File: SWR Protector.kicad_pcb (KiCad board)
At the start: 2 copper layers, 100 x 100 mm, 34 parts, among them J1 Barrel_Jack, J2 Barrel_Jack, J3 transceiver, J4 antenna, J5 header, K2 ATX209, Q1 2N3904, T1 1:12, T2 1:12, U1 LM78L05_TO92, U2 LM358

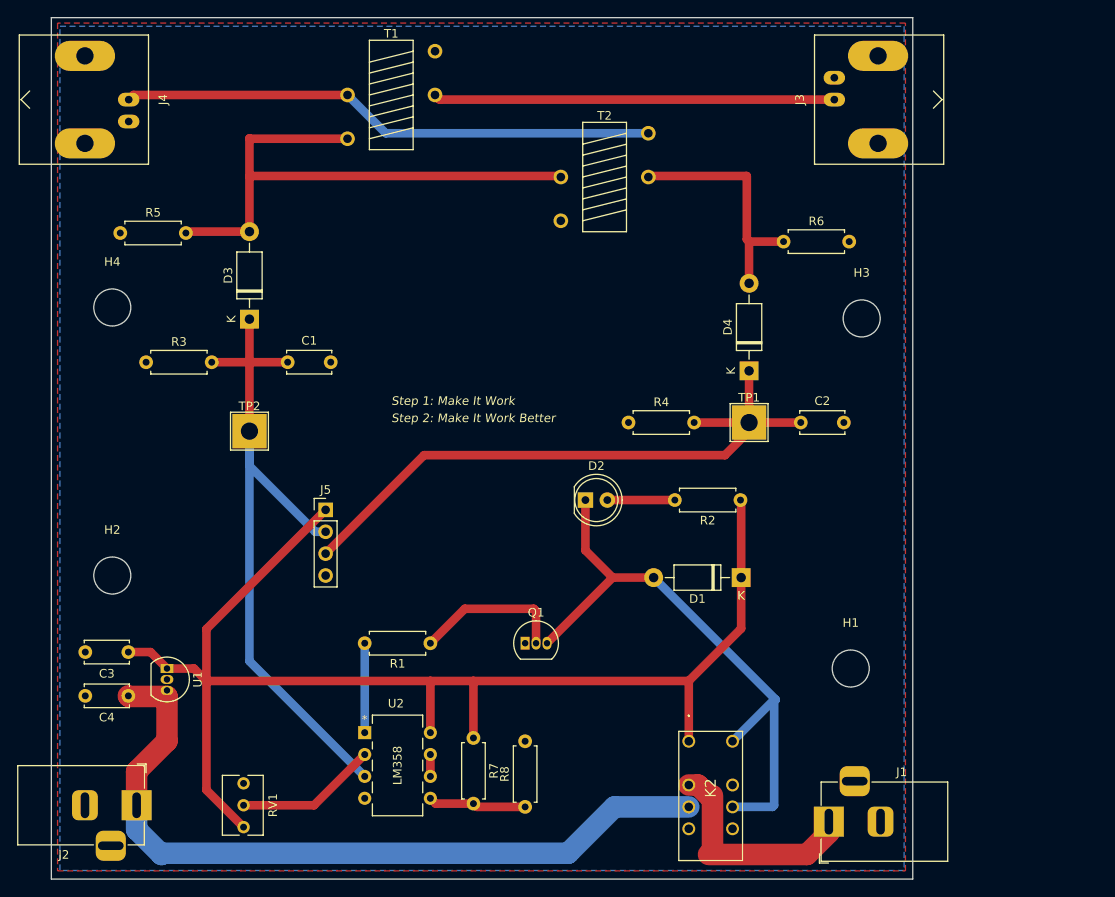
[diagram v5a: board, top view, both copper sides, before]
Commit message: learned how to do via stitching, but the array lands over everything so I spent a lot of time finding and fixing errors (ground via punching right thru power trace, for instance).  Next time the via stitching MUST BE THE LAST STEP IN BOARD DESIGN as any changes at this point will be painful.
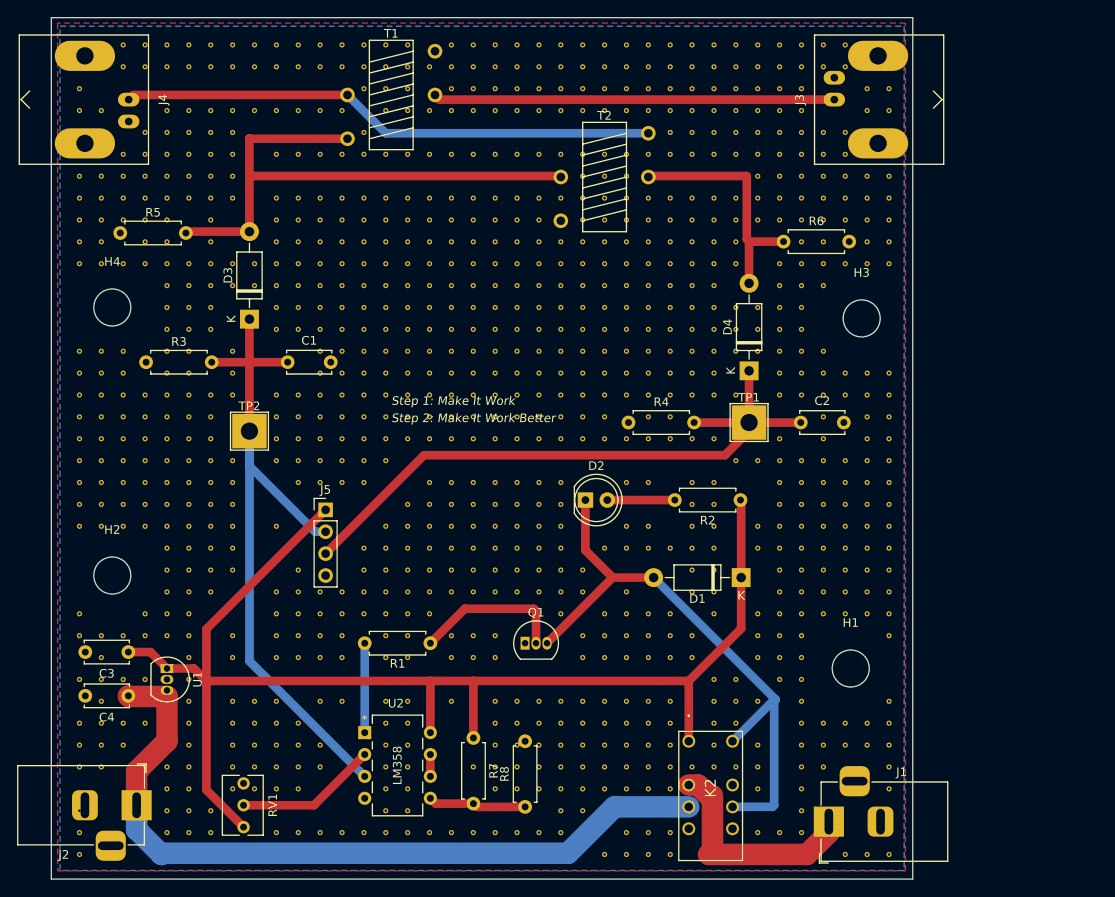
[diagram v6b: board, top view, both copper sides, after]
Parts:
- added REF**10: VIA-0.6mm, MyLibrary:VIA-0.6mm, F.Cu at (113.7, 50.2)
- added REF**100: VIA-0.6mm, MyLibrary:VIA-0.6mm, F.Cu at (149.2, 55.2)
- added REF**1000: VIA-0.6mm, MyLibrary:VIA-0.6mm, F.Cu at (118.7, 116.2)
- added REF**1001: VIA-0.6mm, MyLibrary:VIA-0.6mm, F.Cu at (121.3, 116.2)
- added REF**1002: VIA-0.6mm, MyLibrary:VIA-0.6mm, F.Cu at (123.8, 116.2)
- added REF**1003: VIA-0.6mm, MyLibrary:VIA-0.6mm, F.Cu at (126.4, 116.2)
- added REF**1004: VIA-0.6mm, MyLibrary:VIA-0.6mm, F.Cu at (128.9, 116.2)
- added REF**101: VIA-0.6mm, MyLibrary:VIA-0.6mm, F.Cu at (151.8, 55.2)
- added REF**1010: VIA-0.6mm, MyLibrary:VIA-0.6mm, F.Cu at (144.1, 116.2)
- added REF**1012: VIA-0.6mm, MyLibrary:VIA-0.6mm, F.Cu at (149.2, 116.2)
- added REF**1013: VIA-0.6mm, MyLibrary:VIA-0.6mm, F.Cu at (151.8, 116.2)
- added REF**1014: VIA-0.6mm, MyLibrary:VIA-0.6mm, F.Cu at (154.3, 116.2)
- added REF**1015: VIA-0.6mm, MyLibrary:VIA-0.6mm, F.Cu at (156.8, 116.2)
- added REF**1017: VIA-0.6mm, MyLibrary:VIA-0.6mm, F.Cu at (161.9, 116.2)
- added REF**1019: VIA-0.6mm, MyLibrary:VIA-0.6mm, F.Cu at (167.0, 116.2)
- added REF**102: VIA-0.6mm, MyLibrary:VIA-0.6mm, F.Cu at (154.3, 55.2)
- added REF**1020: VIA-0.6mm, MyLibrary:VIA-0.6mm, F.Cu at (169.5, 116.2)
- added REF**1021: VIA-0.6mm, MyLibrary:VIA-0.6mm, F.Cu at (172.1, 116.2)
- added REF**1022: VIA-0.6mm, MyLibrary:VIA-0.6mm, F.Cu at (174.6, 116.2)
- added REF**1023: VIA-0.6mm, MyLibrary:VIA-0.6mm, F.Cu at (177.2, 116.2)
- added REF**1024: VIA-0.6mm, MyLibrary:VIA-0.6mm, F.Cu at (179.7, 116.2)
- added REF**1025: VIA-0.6mm, MyLibrary:VIA-0.6mm, F.Cu at (182.2, 116.2)
- added REF**1026: VIA-0.6mm, MyLibrary:VIA-0.6mm, F.Cu at (88.3, 118.7)
- added REF**1027: VIA-0.6mm, MyLibrary:VIA-0.6mm, F.Cu at (90.8, 118.7)
- added REF**1028: VIA-0.6mm, MyLibrary:VIA-0.6mm, F.Cu at (93.3, 118.7)
- added REF**1029: VIA-0.6mm, MyLibrary:VIA-0.6mm, F.Cu at (95.9, 118.7)
- added REF**103: VIA-0.6mm, MyLibrary:VIA-0.6mm, F.Cu at (156.8, 55.2)
- added REF**1030: VIA-0.6mm, MyLibrary:VIA-0.6mm, F.Cu at (98.4, 118.7)
- added REF**1031: VIA-0.6mm, MyLibrary:VIA-0.6mm, F.Cu at (101.0, 118.7)
- added REF**1033: VIA-0.6mm, MyLibrary:VIA-0.6mm, F.Cu at (106.0, 118.7)
- added REF**1035: VIA-0.6mm, MyLibrary:VIA-0.6mm, F.Cu at (111.1, 118.7)
- added REF**1036: VIA-0.6mm, MyLibrary:VIA-0.6mm, F.Cu at (113.7, 118.7)
- added REF**1037: VIA-0.6mm, MyLibrary:VIA-0.6mm, F.Cu at (116.2, 118.7)
- added REF**1038: VIA-0.6mm, MyLibrary:VIA-0.6mm, F.Cu at (118.7, 118.7)
- added REF**104: VIA-0.6mm, MyLibrary:VIA-0.6mm, F.Cu at (159.4, 55.2)
- added REF**1040: VIA-0.6mm, MyLibrary:VIA-0.6mm, F.Cu at (123.8, 118.7)
- added REF**1041: VIA-0.6mm, MyLibrary:VIA-0.6mm, F.Cu at (126.4, 118.7)
- added REF**1043: VIA-0.6mm, MyLibrary:VIA-0.6mm, F.Cu at (131.4, 118.7)
- added REF**1044: VIA-0.6mm, MyLibrary:VIA-0.6mm, F.Cu at (134.0, 118.7)
- added REF**1045: VIA-0.6mm, MyLibrary:VIA-0.6mm, F.Cu at (136.5, 118.7)
- added REF**1049: VIA-0.6mm, MyLibrary:VIA-0.6mm, F.Cu at (146.7, 118.7)
- added REF**105: VIA-0.6mm, MyLibrary:VIA-0.6mm, F.Cu at (161.9, 55.2)
- added REF**1050: VIA-0.6mm, MyLibrary:VIA-0.6mm, F.Cu at (149.2, 118.7)
- added REF**1051: VIA-0.6mm, MyLibrary:VIA-0.6mm, F.Cu at (151.8, 118.7)
- added REF**1052: VIA-0.6mm, MyLibrary:VIA-0.6mm, F.Cu at (154.3, 118.7)
- added REF**1053: VIA-0.6mm, MyLibrary:VIA-0.6mm, F.Cu at (156.8, 118.7)
- added REF**1054: VIA-0.6mm, MyLibrary:VIA-0.6mm, F.Cu at (159.4, 118.7)
- added REF**1057: VIA-0.6mm, MyLibrary:VIA-0.6mm, F.Cu at (167.0, 118.7)
- added REF**1058: VIA-0.6mm, MyLibrary:VIA-0.6mm, F.Cu at (169.5, 118.7)
- added REF**1059: VIA-0.6mm, MyLibrary:VIA-0.6mm, F.Cu at (172.1, 118.7)
- added REF**106: VIA-0.6mm, MyLibrary:VIA-0.6mm, F.Cu at (164.5, 55.2)
- added REF**1063: VIA-0.6mm, MyLibrary:VIA-0.6mm, F.Cu at (182.2, 118.7)
- added REF**1065: VIA-0.6mm, MyLibrary:VIA-0.6mm, F.Cu at (90.8, 121.3)
- added REF**1069: VIA-0.6mm, MyLibrary:VIA-0.6mm, F.Cu at (101.0, 121.3)
- added REF**107: VIA-0.6mm, MyLibrary:VIA-0.6mm, F.Cu at (167.0, 55.2)
- added REF**1071: VIA-0.6mm, MyLibrary:VIA-0.6mm, F.Cu at (106.0, 121.3)
- added REF**1073: VIA-0.6mm, MyLibrary:VIA-0.6mm, F.Cu at (111.1, 121.3)
- added REF**1074: VIA-0.6mm, MyLibrary:VIA-0.6mm, F.Cu at (113.7, 121.3)
- added REF**1075: VIA-0.6mm, MyLibrary:VIA-0.6mm, F.Cu at (116.2, 121.3)
- added REF**1076: VIA-0.6mm, MyLibrary:VIA-0.6mm, F.Cu at (118.7, 121.3)
- added REF**1078: VIA-0.6mm, MyLibrary:VIA-0.6mm, F.Cu at (123.8, 121.3)
- added REF**1079: VIA-0.6mm, MyLibrary:VIA-0.6mm, F.Cu at (126.4, 121.3)
- added REF**108: VIA-0.6mm, MyLibrary:VIA-0.6mm, F.Cu at (169.5, 55.2)
- added REF**1081: VIA-0.6mm, MyLibrary:VIA-0.6mm, F.Cu at (131.4, 121.3)
- added REF**1082: VIA-0.6mm, MyLibrary:VIA-0.6mm, F.Cu at (134.0, 121.3)
- added REF**1083: VIA-0.6mm, MyLibrary:VIA-0.6mm, F.Cu at (136.5, 121.3)
- added REF**1087: VIA-0.6mm, MyLibrary:VIA-0.6mm, F.Cu at (146.7, 121.3)
- added REF**1088: VIA-0.6mm, MyLibrary:VIA-0.6mm, F.Cu at (149.2, 121.3)
- added REF**1089: VIA-0.6mm, MyLibrary:VIA-0.6mm, F.Cu at (151.8, 121.3)
- added REF**109: VIA-0.6mm, MyLibrary:VIA-0.6mm, F.Cu at (172.1, 55.2)
- added REF**1090: VIA-0.6mm, MyLibrary:VIA-0.6mm, F.Cu at (154.3, 121.3)
- added REF**1091: VIA-0.6mm, MyLibrary:VIA-0.6mm, F.Cu at (156.8, 121.3)
- added REF**1092: VIA-0.6mm, MyLibrary:VIA-0.6mm, F.Cu at (159.4, 121.3)
- added REF**1095: VIA-0.6mm, MyLibrary:VIA-0.6mm, F.Cu at (167.0, 121.3)
- added REF**1096: VIA-0.6mm, MyLibrary:VIA-0.6mm, F.Cu at (169.5, 121.3)
- added REF**1097: VIA-0.6mm, MyLibrary:VIA-0.6mm, F.Cu at (172.1, 121.3)
- added REF**11: VIA-0.6mm, MyLibrary:VIA-0.6mm, F.Cu at (116.2, 50.2)
- added REF**1102: VIA-0.6mm, MyLibrary:VIA-0.6mm, F.Cu at (88.3, 123.8)
- added REF**1103: VIA-0.6mm, MyLibrary:VIA-0.6mm, F.Cu at (90.8, 123.8)
- added REF**1104: VIA-0.6mm, MyLibrary:VIA-0.6mm, F.Cu at (93.3, 123.8)
- added REF**1105: VIA-0.6mm, MyLibrary:VIA-0.6mm, F.Cu at (95.9, 123.8)
- added REF**1107: VIA-0.6mm, MyLibrary:VIA-0.6mm, F.Cu at (101.0, 123.8)
- added REF**112: VIA-0.6mm, MyLibrary:VIA-0.6mm, F.Cu at (179.7, 55.2)
- added REF**113: VIA-0.6mm, MyLibrary:VIA-0.6mm, F.Cu at (182.2, 55.2)
- added REF**1131: VIA-0.6mm, MyLibrary:VIA-0.6mm, F.Cu at (161.9, 123.8)
- added REF**1132: VIA-0.6mm, MyLibrary:VIA-0.6mm, F.Cu at (164.5, 123.8)
- added REF**1134: VIA-0.6mm, MyLibrary:VIA-0.6mm, F.Cu at (169.5, 123.8)
- added REF**1135: VIA-0.6mm, MyLibrary:VIA-0.6mm, F.Cu at (172.1, 123.8)
- added REF**114: VIA-0.6mm, MyLibrary:VIA-0.6mm, F.Cu at (88.3, 57.8)
- added REF**1141: VIA-0.6mm, MyLibrary:VIA-0.6mm, F.Cu at (90.8, 126.4)
- added REF**1145: VIA-0.6mm, MyLibrary:VIA-0.6mm, F.Cu at (101.0, 126.4)
- added REF**1147: VIA-0.6mm, MyLibrary:VIA-0.6mm, F.Cu at (106.0, 126.4)
- added REF**1148: VIA-0.6mm, MyLibrary:VIA-0.6mm, F.Cu at (108.6, 126.4)
- added REF**1149: VIA-0.6mm, MyLibrary:VIA-0.6mm, F.Cu at (111.1, 126.4)
- added REF**115: VIA-0.6mm, MyLibrary:VIA-0.6mm, F.Cu at (90.8, 57.8)
- added REF**1151: VIA-0.6mm, MyLibrary:VIA-0.6mm, F.Cu at (116.2, 126.4)
- added REF**1152: VIA-0.6mm, MyLibrary:VIA-0.6mm, F.Cu at (118.7, 126.4)
- added REF**1154: VIA-0.6mm, MyLibrary:VIA-0.6mm, F.Cu at (123.8, 126.4)
- added REF**1155: VIA-0.6mm, MyLibrary:VIA-0.6mm, F.Cu at (126.4, 126.4)
- added REF**1157: VIA-0.6mm, MyLibrary:VIA-0.6mm, F.Cu at (131.4, 126.4)
- added REF**1159: VIA-0.6mm, MyLibrary:VIA-0.6mm, F.Cu at (136.5, 126.4)
- added REF**1160: VIA-0.6mm, MyLibrary:VIA-0.6mm, F.Cu at (139.1, 126.4)
- added REF**1161: VIA-0.6mm, MyLibrary:VIA-0.6mm, F.Cu at (141.6, 126.4)
- added REF**1162: VIA-0.6mm, MyLibrary:VIA-0.6mm, F.Cu at (144.1, 126.4)
- added REF**1163: VIA-0.6mm, MyLibrary:VIA-0.6mm, F.Cu at (146.7, 126.4)
- added REF**1164: VIA-0.6mm, MyLibrary:VIA-0.6mm, F.Cu at (149.2, 126.4)
- added REF**1165: VIA-0.6mm, MyLibrary:VIA-0.6mm, F.Cu at (151.8, 126.4)
- added REF**1166: VIA-0.6mm, MyLibrary:VIA-0.6mm, F.Cu at (154.3, 126.4)
- added REF**1167: VIA-0.6mm, MyLibrary:VIA-0.6mm, F.Cu at (156.8, 126.4)
- added REF**1169: VIA-0.6mm, MyLibrary:VIA-0.6mm, F.Cu at (161.9, 126.4)
- added REF**1170: VIA-0.6mm, MyLibrary:VIA-0.6mm, F.Cu at (164.5, 126.4)
- added REF**1171: VIA-0.6mm, MyLibrary:VIA-0.6mm, F.Cu at (167.0, 126.4)
- added REF**1173: VIA-0.6mm, MyLibrary:VIA-0.6mm, F.Cu at (172.1, 126.4)
- added REF**1177: VIA-0.6mm, MyLibrary:VIA-0.6mm, F.Cu at (182.2, 126.4)
- added REF**1178: VIA-0.6mm, MyLibrary:VIA-0.6mm, F.Cu at (88.3, 128.9)
- added REF**1179: VIA-0.6mm, MyLibrary:VIA-0.6mm, F.Cu at (90.8, 128.9)
- added REF**118: VIA-0.6mm, MyLibrary:VIA-0.6mm, F.Cu at (98.4, 57.8)
- added REF**1180: VIA-0.6mm, MyLibrary:VIA-0.6mm, F.Cu at (93.3, 128.9)
- added REF**1181: VIA-0.6mm, MyLibrary:VIA-0.6mm, F.Cu at (95.9, 128.9)
- added REF**1183: VIA-0.6mm, MyLibrary:VIA-0.6mm, F.Cu at (101.0, 128.9)
- added REF**1185: VIA-0.6mm, MyLibrary:VIA-0.6mm, F.Cu at (106.0, 128.9)
- added REF**1186: VIA-0.6mm, MyLibrary:VIA-0.6mm, F.Cu at (108.6, 128.9)
- added REF**1187: VIA-0.6mm, MyLibrary:VIA-0.6mm, F.Cu at (111.1, 128.9)
- added REF**1188: VIA-0.6mm, MyLibrary:VIA-0.6mm, F.Cu at (113.7, 128.9)
- added REF**119: VIA-0.6mm, MyLibrary:VIA-0.6mm, F.Cu at (101.0, 57.8)
- added REF**1192: VIA-0.6mm, MyLibrary:VIA-0.6mm, F.Cu at (123.8, 128.9)
- added REF**1193: VIA-0.6mm, MyLibrary:VIA-0.6mm, F.Cu at (126.4, 128.9)
- added REF**1197: VIA-0.6mm, MyLibrary:VIA-0.6mm, F.Cu at (136.5, 128.9)
- added REF**1198: VIA-0.6mm, MyLibrary:VIA-0.6mm, F.Cu at (139.1, 128.9)
- added REF**1199: VIA-0.6mm, MyLibrary:VIA-0.6mm, F.Cu at (141.6, 128.9)
- added REF**12: VIA-0.6mm, MyLibrary:VIA-0.6mm, F.Cu at (118.7, 50.2)
- added REF**120: VIA-0.6mm, MyLibrary:VIA-0.6mm, F.Cu at (103.5, 57.8)
- added REF**1200: VIA-0.6mm, MyLibrary:VIA-0.6mm, F.Cu at (144.1, 128.9)
- added REF**1201: VIA-0.6mm, MyLibrary:VIA-0.6mm, F.Cu at (146.7, 128.9)
- added REF**1202: VIA-0.6mm, MyLibrary:VIA-0.6mm, F.Cu at (149.2, 128.9)
- added REF**1203: VIA-0.6mm, MyLibrary:VIA-0.6mm, F.Cu at (151.8, 128.9)
- added REF**1204: VIA-0.6mm, MyLibrary:VIA-0.6mm, F.Cu at (154.3, 128.9)
- added REF**1205: VIA-0.6mm, MyLibrary:VIA-0.6mm, F.Cu at (156.8, 128.9)
- added REF**1207: VIA-0.6mm, MyLibrary:VIA-0.6mm, F.Cu at (161.9, 128.9)
- added REF**1208: VIA-0.6mm, MyLibrary:VIA-0.6mm, F.Cu at (164.5, 128.9)
- added REF**121: VIA-0.6mm, MyLibrary:VIA-0.6mm, F.Cu at (106.0, 57.8)
- added REF**1211: VIA-0.6mm, MyLibrary:VIA-0.6mm, F.Cu at (172.1, 128.9)
- added REF**1212: VIA-0.6mm, MyLibrary:VIA-0.6mm, F.Cu at (174.6, 128.9)
- added REF**1213: VIA-0.6mm, MyLibrary:VIA-0.6mm, F.Cu at (177.2, 128.9)
- added REF**1214: VIA-0.6mm, MyLibrary:VIA-0.6mm, F.Cu at (179.7, 128.9)
- added REF**1215: VIA-0.6mm, MyLibrary:VIA-0.6mm, F.Cu at (182.2, 128.9)
- added REF**1216: VIA-0.6mm, MyLibrary:VIA-0.6mm, F.Cu at (88.3, 131.4)
- added REF**1217: VIA-0.6mm, MyLibrary:VIA-0.6mm, F.Cu at (90.8, 131.4)
- added REF**1218: VIA-0.6mm, MyLibrary:VIA-0.6mm, F.Cu at (93.3, 131.4)
- added REF**122: VIA-0.6mm, MyLibrary:VIA-0.6mm, F.Cu at (108.6, 57.8)
- added REF**1221: VIA-0.6mm, MyLibrary:VIA-0.6mm, F.Cu at (101.0, 131.4)
- added REF**1223: VIA-0.6mm, MyLibrary:VIA-0.6mm, F.Cu at (106.0, 131.4)
- added REF**1224: VIA-0.6mm, MyLibrary:VIA-0.6mm, F.Cu at (108.6, 131.4)
- added REF**1225: VIA-0.6mm, MyLibrary:VIA-0.6mm, F.Cu at (111.1, 131.4)
- added REF**1226: VIA-0.6mm, MyLibrary:VIA-0.6mm, F.Cu at (113.7, 131.4)
- added REF**1227: VIA-0.6mm, MyLibrary:VIA-0.6mm, F.Cu at (116.2, 131.4)
- added REF**123: VIA-0.6mm, MyLibrary:VIA-0.6mm, F.Cu at (111.1, 57.8)
- added REF**1230: VIA-0.6mm, MyLibrary:VIA-0.6mm, F.Cu at (123.8, 131.4)
- added REF**1231: VIA-0.6mm, MyLibrary:VIA-0.6mm, F.Cu at (126.4, 131.4)
- added REF**1235: VIA-0.6mm, MyLibrary:VIA-0.6mm, F.Cu at (136.5, 131.4)
- added REF**1236: VIA-0.6mm, MyLibrary:VIA-0.6mm, F.Cu at (139.1, 131.4)
- added REF**1237: VIA-0.6mm, MyLibrary:VIA-0.6mm, F.Cu at (141.6, 131.4)
- added REF**1238: VIA-0.6mm, MyLibrary:VIA-0.6mm, F.Cu at (144.1, 131.4)
- added REF**1239: VIA-0.6mm, MyLibrary:VIA-0.6mm, F.Cu at (146.7, 131.4)
- added REF**124: VIA-0.6mm, MyLibrary:VIA-0.6mm, F.Cu at (113.7, 57.8)
- added REF**1240: VIA-0.6mm, MyLibrary:VIA-0.6mm, F.Cu at (149.2, 131.4)
- added REF**1241: VIA-0.6mm, MyLibrary:VIA-0.6mm, F.Cu at (151.8, 131.4)
- added REF**1242: VIA-0.6mm, MyLibrary:VIA-0.6mm, F.Cu at (154.3, 131.4)
- added REF**1243: VIA-0.6mm, MyLibrary:VIA-0.6mm, F.Cu at (156.8, 131.4)
- added REF**1245: VIA-0.6mm, MyLibrary:VIA-0.6mm, F.Cu at (161.9, 131.4)
- added REF**1247: VIA-0.6mm, MyLibrary:VIA-0.6mm, F.Cu at (167.0, 131.4)
- added REF**1249: VIA-0.6mm, MyLibrary:VIA-0.6mm, F.Cu at (172.1, 131.4)
- added REF**125: VIA-0.6mm, MyLibrary:VIA-0.6mm, F.Cu at (116.2, 57.8)
- added REF**1250: VIA-0.6mm, MyLibrary:VIA-0.6mm, F.Cu at (174.6, 131.4)
- added REF**1251: VIA-0.6mm, MyLibrary:VIA-0.6mm, F.Cu at (177.2, 131.4)
- added REF**1252: VIA-0.6mm, MyLibrary:VIA-0.6mm, F.Cu at (179.7, 131.4)
- added REF**1253: VIA-0.6mm, MyLibrary:VIA-0.6mm, F.Cu at (182.2, 131.4)
- added REF**1254: VIA-0.6mm, MyLibrary:VIA-0.6mm, F.Cu at (88.3, 134.0)
- added REF**1255: VIA-0.6mm, MyLibrary:VIA-0.6mm, F.Cu at (90.8, 134.0)
- added REF**1258: VIA-0.6mm, MyLibrary:VIA-0.6mm, F.Cu at (98.4, 134.0)
- added REF**1259: VIA-0.6mm, MyLibrary:VIA-0.6mm, F.Cu at (101.0, 134.0)
- added REF**126: VIA-0.6mm, MyLibrary:VIA-0.6mm, F.Cu at (118.7, 57.8)
- added REF**1261: VIA-0.6mm, MyLibrary:VIA-0.6mm, F.Cu at (106.0, 134.0)
- added REF**1262: VIA-0.6mm, MyLibrary:VIA-0.6mm, F.Cu at (108.6, 134.0)
- added REF**1263: VIA-0.6mm, MyLibrary:VIA-0.6mm, F.Cu at (111.1, 134.0)
- added REF**1264: VIA-0.6mm, MyLibrary:VIA-0.6mm, F.Cu at (113.7, 134.0)
- added REF**1265: VIA-0.6mm, MyLibrary:VIA-0.6mm, F.Cu at (116.2, 134.0)
- added REF**1268: VIA-0.6mm, MyLibrary:VIA-0.6mm, F.Cu at (123.8, 134.0)
- added REF**1269: VIA-0.6mm, MyLibrary:VIA-0.6mm, F.Cu at (126.4, 134.0)
- added REF**1272: VIA-0.6mm, MyLibrary:VIA-0.6mm, F.Cu at (134.0, 134.0)
- added REF**1273: VIA-0.6mm, MyLibrary:VIA-0.6mm, F.Cu at (136.5, 134.0)
- added REF**1274: VIA-0.6mm, MyLibrary:VIA-0.6mm, F.Cu at (139.1, 134.0)
- added REF**1275: VIA-0.6mm, MyLibrary:VIA-0.6mm, F.Cu at (141.6, 134.0)
- added REF**1276: VIA-0.6mm, MyLibrary:VIA-0.6mm, F.Cu at (144.1, 134.0)
- added REF**1277: VIA-0.6mm, MyLibrary:VIA-0.6mm, F.Cu at (146.7, 134.0)
- added REF**1278: VIA-0.6mm, MyLibrary:VIA-0.6mm, F.Cu at (149.2, 134.0)
- added REF**1279: VIA-0.6mm, MyLibrary:VIA-0.6mm, F.Cu at (151.8, 134.0)
- added REF**128: VIA-0.6mm, MyLibrary:VIA-0.6mm, F.Cu at (123.8, 57.8)
- added REF**1280: VIA-0.6mm, MyLibrary:VIA-0.6mm, F.Cu at (154.3, 134.0)
- added REF**1281: VIA-0.6mm, MyLibrary:VIA-0.6mm, F.Cu at (156.8, 134.0)
- added REF**1282: VIA-0.6mm, MyLibrary:VIA-0.6mm, F.Cu at (159.4, 134.0)
- added REF**1283: VIA-0.6mm, MyLibrary:VIA-0.6mm, F.Cu at (161.9, 134.0)
- added REF**1284: VIA-0.6mm, MyLibrary:VIA-0.6mm, F.Cu at (164.5, 134.0)
- added REF**1285: VIA-0.6mm, MyLibrary:VIA-0.6mm, F.Cu at (167.0, 134.0)
- added REF**1287: VIA-0.6mm, MyLibrary:VIA-0.6mm, F.Cu at (172.1, 134.0)
- added REF**1288: VIA-0.6mm, MyLibrary:VIA-0.6mm, F.Cu at (174.6, 134.0)
- added REF**129: VIA-0.6mm, MyLibrary:VIA-0.6mm, F.Cu at (126.4, 57.8)
- added REF**1291: VIA-0.6mm, MyLibrary:VIA-0.6mm, F.Cu at (182.2, 134.0)
- added REF**1296: VIA-0.6mm, MyLibrary:VIA-0.6mm, F.Cu at (98.4, 136.5)
- added REF**1297: VIA-0.6mm, MyLibrary:VIA-0.6mm, F.Cu at (101.0, 136.5)
- added REF**1299: VIA-0.6mm, MyLibrary:VIA-0.6mm, F.Cu at (106.0, 136.5)
- added REF**13: VIA-0.6mm, MyLibrary:VIA-0.6mm, F.Cu at (121.3, 50.2)
- added REF**130: VIA-0.6mm, MyLibrary:VIA-0.6mm, F.Cu at (128.9, 57.8)
- added REF**1300: VIA-0.6mm, MyLibrary:VIA-0.6mm, F.Cu at (108.6, 136.5)
- added REF**1301: VIA-0.6mm, MyLibrary:VIA-0.6mm, F.Cu at (111.1, 136.5)
- added REF**1302: VIA-0.6mm, MyLibrary:VIA-0.6mm, F.Cu at (113.7, 136.5)
- added REF**1306: VIA-0.6mm, MyLibrary:VIA-0.6mm, F.Cu at (123.8, 136.5)
- added REF**1307: VIA-0.6mm, MyLibrary:VIA-0.6mm, F.Cu at (126.4, 136.5)
- added REF**131: VIA-0.6mm, MyLibrary:VIA-0.6mm, F.Cu at (131.4, 57.8)
- added REF**1311: VIA-0.6mm, MyLibrary:VIA-0.6mm, F.Cu at (136.5, 136.5)
- added REF**1312: VIA-0.6mm, MyLibrary:VIA-0.6mm, F.Cu at (139.1, 136.5)
- added REF**1313: VIA-0.6mm, MyLibrary:VIA-0.6mm, F.Cu at (141.6, 136.5)
- added REF**1314: VIA-0.6mm, MyLibrary:VIA-0.6mm, F.Cu at (144.1, 136.5)
- added REF**1315: VIA-0.6mm, MyLibrary:VIA-0.6mm, F.Cu at (146.7, 136.5)
- added REF**1316: VIA-0.6mm, MyLibrary:VIA-0.6mm, F.Cu at (149.2, 136.5)
- added REF**1317: VIA-0.6mm, MyLibrary:VIA-0.6mm, F.Cu at (151.8, 136.5)
- added REF**1318: VIA-0.6mm, MyLibrary:VIA-0.6mm, F.Cu at (154.3, 136.5)
- added REF**1319: VIA-0.6mm, MyLibrary:VIA-0.6mm, F.Cu at (156.8, 136.5)
- added REF**132: VIA-0.6mm, MyLibrary:VIA-0.6mm, F.Cu at (134.0, 57.8)
- added REF**1323: VIA-0.6mm, MyLibrary:VIA-0.6mm, F.Cu at (167.0, 136.5)
- added REF**1325: VIA-0.6mm, MyLibrary:VIA-0.6mm, F.Cu at (172.1, 136.5)
- added REF**1329: VIA-0.6mm, MyLibrary:VIA-0.6mm, F.Cu at (182.2, 136.5)
- added REF**133: VIA-0.6mm, MyLibrary:VIA-0.6mm, F.Cu at (136.5, 57.8)
- added REF**1330: VIA-0.6mm, MyLibrary:VIA-0.6mm, F.Cu at (88.3, 139.1)
- added REF**1334: VIA-0.6mm, MyLibrary:VIA-0.6mm, F.Cu at (98.4, 139.1)
- added REF**1335: VIA-0.6mm, MyLibrary:VIA-0.6mm, F.Cu at (101.0, 139.1)
- added REF**1336: VIA-0.6mm, MyLibrary:VIA-0.6mm, F.Cu at (103.5, 139.1)
- added REF**134: VIA-0.6mm, MyLibrary:VIA-0.6mm, F.Cu at (139.1, 57.8)
- added REF**1344: VIA-0.6mm, MyLibrary:VIA-0.6mm, F.Cu at (123.8, 139.1)
- added REF**1345: VIA-0.6mm, MyLibrary:VIA-0.6mm, F.Cu at (126.4, 139.1)
- added REF**135: VIA-0.6mm, MyLibrary:VIA-0.6mm, F.Cu at (141.6, 57.8)
- added REF**1352: VIA-0.6mm, MyLibrary:VIA-0.6mm, F.Cu at (144.1, 139.1)
- added REF**1353: VIA-0.6mm, MyLibrary:VIA-0.6mm, F.Cu at (146.7, 139.1)
- added REF**136: VIA-0.6mm, MyLibrary:VIA-0.6mm, F.Cu at (144.1, 57.8)
- added REF**1363: VIA-0.6mm, MyLibrary:VIA-0.6mm, F.Cu at (172.1, 139.1)
- added REF**1368: VIA-0.6mm, MyLibrary:VIA-0.6mm, F.Cu at (88.3, 141.6)
- added REF**137: VIA-0.6mm, MyLibrary:VIA-0.6mm, F.Cu at (146.7, 57.8)
- added REF**1372: VIA-0.6mm, MyLibrary:VIA-0.6mm, F.Cu at (98.4, 141.6)
- added REF**1373: VIA-0.6mm, MyLibrary:VIA-0.6mm, F.Cu at (101.0, 141.6)
- added REF**1374: VIA-0.6mm, MyLibrary:VIA-0.6mm, F.Cu at (103.5, 141.6)
- added REF**1377: VIA-0.6mm, MyLibrary:VIA-0.6mm, F.Cu at (111.1, 141.6)
- added REF**1378: VIA-0.6mm, MyLibrary:VIA-0.6mm, F.Cu at (113.7, 141.6)
- added REF**1379: VIA-0.6mm, MyLibrary:VIA-0.6mm, F.Cu at (116.2, 141.6)
- added REF**138: VIA-0.6mm, MyLibrary:VIA-0.6mm, F.Cu at (149.2, 57.8)
- added REF**1380: VIA-0.6mm, MyLibrary:VIA-0.6mm, F.Cu at (118.7, 141.6)
- added REF**1381: VIA-0.6mm, MyLibrary:VIA-0.6mm, F.Cu at (121.3, 141.6)
- added REF**1382: VIA-0.6mm, MyLibrary:VIA-0.6mm, F.Cu at (123.8, 141.6)
- added REF**1383: VIA-0.6mm, MyLibrary:VIA-0.6mm, F.Cu at (126.4, 141.6)
- added REF**1384: VIA-0.6mm, MyLibrary:VIA-0.6mm, F.Cu at (128.9, 141.6)
- added REF**1385: VIA-0.6mm, MyLibrary:VIA-0.6mm, F.Cu at (131.4, 141.6)
- added REF**1386: VIA-0.6mm, MyLibrary:VIA-0.6mm, F.Cu at (134.0, 141.6)
- added REF**1387: VIA-0.6mm, MyLibrary:VIA-0.6mm, F.Cu at (136.5, 141.6)
- added REF**1388: VIA-0.6mm, MyLibrary:VIA-0.6mm, F.Cu at (139.1, 141.6)
- added REF**1389: VIA-0.6mm, MyLibrary:VIA-0.6mm, F.Cu at (141.6, 141.6)
- added REF**139: VIA-0.6mm, MyLibrary:VIA-0.6mm, F.Cu at (151.8, 57.8)
- added REF**1390: VIA-0.6mm, MyLibrary:VIA-0.6mm, F.Cu at (144.1, 141.6)
- added REF**1393: VIA-0.6mm, MyLibrary:VIA-0.6mm, F.Cu at (151.8, 141.6)
- added REF**1394: VIA-0.6mm, MyLibrary:VIA-0.6mm, F.Cu at (154.3, 141.6)
- added REF**1395: VIA-0.6mm, MyLibrary:VIA-0.6mm, F.Cu at (156.8, 141.6)
- added REF**1399: VIA-0.6mm, MyLibrary:VIA-0.6mm, F.Cu at (167.0, 141.6)
- added REF**14: VIA-0.6mm, MyLibrary:VIA-0.6mm, F.Cu at (123.8, 50.2)
- added REF**140: VIA-0.6mm, MyLibrary:VIA-0.6mm, F.Cu at (154.3, 57.8)
- added REF**1400: VIA-0.6mm, MyLibrary:VIA-0.6mm, F.Cu at (169.5, 141.6)
- added REF**1401: VIA-0.6mm, MyLibrary:VIA-0.6mm, F.Cu at (172.1, 141.6)
- added REF**1406: VIA-0.6mm, MyLibrary:VIA-0.6mm, F.Cu at (88.3, 144.1)
- added REF**141: VIA-0.6mm, MyLibrary:VIA-0.6mm, F.Cu at (156.8, 57.8)
- added REF**142: VIA-0.6mm, MyLibrary:VIA-0.6mm, F.Cu at (159.4, 57.8)
- added REF**143: VIA-0.6mm, MyLibrary:VIA-0.6mm, F.Cu at (161.9, 57.8)
- added REF**1430: VIA-0.6mm, MyLibrary:VIA-0.6mm, F.Cu at (149.2, 144.1)
- added REF**1431: VIA-0.6mm, MyLibrary:VIA-0.6mm, F.Cu at (151.8, 144.1)
- added REF**1432: VIA-0.6mm, MyLibrary:VIA-0.6mm, F.Cu at (154.3, 144.1)
- added REF**1433: VIA-0.6mm, MyLibrary:VIA-0.6mm, F.Cu at (156.8, 144.1)
- added REF**144: VIA-0.6mm, MyLibrary:VIA-0.6mm, F.Cu at (164.5, 57.8)
- added REF**1441: VIA-0.6mm, MyLibrary:VIA-0.6mm, F.Cu at (177.2, 144.1)
- added REF**1442: VIA-0.6mm, MyLibrary:VIA-0.6mm, F.Cu at (179.7, 144.1)
- added REF**1443: VIA-0.6mm, MyLibrary:VIA-0.6mm, F.Cu at (182.2, 144.1)
- added REF**145: VIA-0.6mm, MyLibrary:VIA-0.6mm, F.Cu at (167.0, 57.8)
- added REF**146: VIA-0.6mm, MyLibrary:VIA-0.6mm, F.Cu at (169.5, 57.8)
- added REF**147: VIA-0.6mm, MyLibrary:VIA-0.6mm, F.Cu at (172.1, 57.8)
- added REF**15: VIA-0.6mm, MyLibrary:VIA-0.6mm, F.Cu at (126.4, 50.2)
- added REF**150: VIA-0.6mm, MyLibrary:VIA-0.6mm, F.Cu at (179.7, 57.8)
- added REF**151: VIA-0.6mm, MyLibrary:VIA-0.6mm, F.Cu at (182.2, 57.8)
- added REF**155: VIA-0.6mm, MyLibrary:VIA-0.6mm, F.Cu at (95.9, 60.3)
- added REF**156: VIA-0.6mm, MyLibrary:VIA-0.6mm, F.Cu at (98.4, 60.3)
- added REF**157: VIA-0.6mm, MyLibrary:VIA-0.6mm, F.Cu at (101.0, 60.3)
- added REF**158: VIA-0.6mm, MyLibrary:VIA-0.6mm, F.Cu at (103.5, 60.3)
- added REF**159: VIA-0.6mm, MyLibrary:VIA-0.6mm, F.Cu at (106.0, 60.3)
- added REF**165: VIA-0.6mm, MyLibrary:VIA-0.6mm, F.Cu at (121.3, 60.3)
- added REF**17: VIA-0.6mm, MyLibrary:VIA-0.6mm, F.Cu at (131.4, 50.2)
- added REF**179: VIA-0.6mm, MyLibrary:VIA-0.6mm, F.Cu at (156.8, 60.3)
- added REF**18: VIA-0.6mm, MyLibrary:VIA-0.6mm, F.Cu at (134.0, 50.2)
- added REF**180: VIA-0.6mm, MyLibrary:VIA-0.6mm, F.Cu at (159.4, 60.3)
- added REF**181: VIA-0.6mm, MyLibrary:VIA-0.6mm, F.Cu at (161.9, 60.3)
- added REF**182: VIA-0.6mm, MyLibrary:VIA-0.6mm, F.Cu at (164.5, 60.3)
- added REF**183: VIA-0.6mm, MyLibrary:VIA-0.6mm, F.Cu at (167.0, 60.3)
- added REF**184: VIA-0.6mm, MyLibrary:VIA-0.6mm, F.Cu at (169.5, 60.3)
- added REF**185: VIA-0.6mm, MyLibrary:VIA-0.6mm, F.Cu at (172.1, 60.3)
- added REF**186: VIA-0.6mm, MyLibrary:VIA-0.6mm, F.Cu at (174.6, 60.3)
- added REF**187: VIA-0.6mm, MyLibrary:VIA-0.6mm, F.Cu at (177.2, 60.3)
- added REF**19: VIA-0.6mm, MyLibrary:VIA-0.6mm, F.Cu at (136.5, 50.2)
- added REF**192: VIA-0.6mm, MyLibrary:VIA-0.6mm, F.Cu at (93.3, 62.9)
- added REF**193: VIA-0.6mm, MyLibrary:VIA-0.6mm, F.Cu at (95.9, 62.9)
- added REF**194: VIA-0.6mm, MyLibrary:VIA-0.6mm, F.Cu at (98.4, 62.9)
- added REF**195: VIA-0.6mm, MyLibrary:VIA-0.6mm, F.Cu at (101.0, 62.9)
- added REF**196: VIA-0.6mm, MyLibrary:VIA-0.6mm, F.Cu at (103.5, 62.9)
- added REF**197: VIA-0.6mm, MyLibrary:VIA-0.6mm, F.Cu at (106.0, 62.9)
- added REF**199: VIA-0.6mm, MyLibrary:VIA-0.6mm, F.Cu at (111.1, 62.9)
- added REF**2: VIA-0.6mm, MyLibrary:VIA-0.6mm, F.Cu at (93.3, 50.2)
- added REF**20: VIA-0.6mm, MyLibrary:VIA-0.6mm, F.Cu at (139.1, 50.2)
- added REF**200: VIA-0.6mm, MyLibrary:VIA-0.6mm, F.Cu at (113.7, 62.9)
- added REF**201: VIA-0.6mm, MyLibrary:VIA-0.6mm, F.Cu at (116.2, 62.9)
- added REF**202: VIA-0.6mm, MyLibrary:VIA-0.6mm, F.Cu at (118.7, 62.9)
- added REF**203: VIA-0.6mm, MyLibrary:VIA-0.6mm, F.Cu at (121.3, 62.9)
- added REF**204: VIA-0.6mm, MyLibrary:VIA-0.6mm, F.Cu at (123.8, 62.9)
- added REF**205: VIA-0.6mm, MyLibrary:VIA-0.6mm, F.Cu at (126.4, 62.9)
- added REF**206: VIA-0.6mm, MyLibrary:VIA-0.6mm, F.Cu at (128.9, 62.9)
- added REF**207: VIA-0.6mm, MyLibrary:VIA-0.6mm, F.Cu at (131.4, 62.9)
- added REF**208: VIA-0.6mm, MyLibrary:VIA-0.6mm, F.Cu at (134.0, 62.9)
- added REF**209: VIA-0.6mm, MyLibrary:VIA-0.6mm, F.Cu at (136.5, 62.9)
- added REF**21: VIA-0.6mm, MyLibrary:VIA-0.6mm, F.Cu at (141.6, 50.2)
- added REF**210: VIA-0.6mm, MyLibrary:VIA-0.6mm, F.Cu at (139.1, 62.9)
- added REF**211: VIA-0.6mm, MyLibrary:VIA-0.6mm, F.Cu at (141.6, 62.9)
- added REF**212: VIA-0.6mm, MyLibrary:VIA-0.6mm, F.Cu at (144.1, 62.9)
- added REF**213: VIA-0.6mm, MyLibrary:VIA-0.6mm, F.Cu at (146.7, 62.9)
- added REF**214: VIA-0.6mm, MyLibrary:VIA-0.6mm, F.Cu at (149.2, 62.9)
- added REF**215: VIA-0.6mm, MyLibrary:VIA-0.6mm, F.Cu at (151.8, 62.9)
- added REF**216: VIA-0.6mm, MyLibrary:VIA-0.6mm, F.Cu at (154.3, 62.9)
- added REF**217: VIA-0.6mm, MyLibrary:VIA-0.6mm, F.Cu at (156.8, 62.9)
- added REF**218: VIA-0.6mm, MyLibrary:VIA-0.6mm, F.Cu at (159.4, 62.9)
- added REF**219: VIA-0.6mm, MyLibrary:VIA-0.6mm, F.Cu at (161.9, 62.9)
- added REF**22: VIA-0.6mm, MyLibrary:VIA-0.6mm, F.Cu at (144.1, 50.2)
- added REF**220: VIA-0.6mm, MyLibrary:VIA-0.6mm, F.Cu at (164.5, 62.9)
- added REF**221: VIA-0.6mm, MyLibrary:VIA-0.6mm, F.Cu at (167.0, 62.9)
- added REF**222: VIA-0.6mm, MyLibrary:VIA-0.6mm, F.Cu at (169.5, 62.9)
- added REF**223: VIA-0.6mm, MyLibrary:VIA-0.6mm, F.Cu at (172.1, 62.9)
- added REF**224: VIA-0.6mm, MyLibrary:VIA-0.6mm, F.Cu at (174.6, 62.9)
- added REF**225: VIA-0.6mm, MyLibrary:VIA-0.6mm, F.Cu at (177.2, 62.9)
- added REF**228: VIA-0.6mm, MyLibrary:VIA-0.6mm, F.Cu at (88.3, 65.4)
- added REF**229: VIA-0.6mm, MyLibrary:VIA-0.6mm, F.Cu at (90.8, 65.4)
- added REF**23: VIA-0.6mm, MyLibrary:VIA-0.6mm, F.Cu at (146.7, 50.2)
- added REF**230: VIA-0.6mm, MyLibrary:VIA-0.6mm, F.Cu at (93.3, 65.4)
- added REF**231: VIA-0.6mm, MyLibrary:VIA-0.6mm, F.Cu at (95.9, 65.4)
- added REF**232: VIA-0.6mm, MyLibrary:VIA-0.6mm, F.Cu at (98.4, 65.4)
- added REF**233: VIA-0.6mm, MyLibrary:VIA-0.6mm, F.Cu at (101.0, 65.4)
- added REF**234: VIA-0.6mm, MyLibrary:VIA-0.6mm, F.Cu at (103.5, 65.4)
- added REF**235: VIA-0.6mm, MyLibrary:VIA-0.6mm, F.Cu at (106.0, 65.4)
- added REF**24: VIA-0.6mm, MyLibrary:VIA-0.6mm, F.Cu at (149.2, 50.2)
- added REF**25: VIA-0.6mm, MyLibrary:VIA-0.6mm, F.Cu at (151.8, 50.2)
- added REF**251: VIA-0.6mm, MyLibrary:VIA-0.6mm, F.Cu at (146.7, 65.4)
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
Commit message: v0.8 massive changes.  Start with 1593L board, imported schematic, updated symbol libs and footprint libs.  Working on layout now. Dropped testpoints as we have them on the header now.  Diodes and resistors all went vertical to save space.  LED is horizontal so it pokes out the faceplate near switched power.
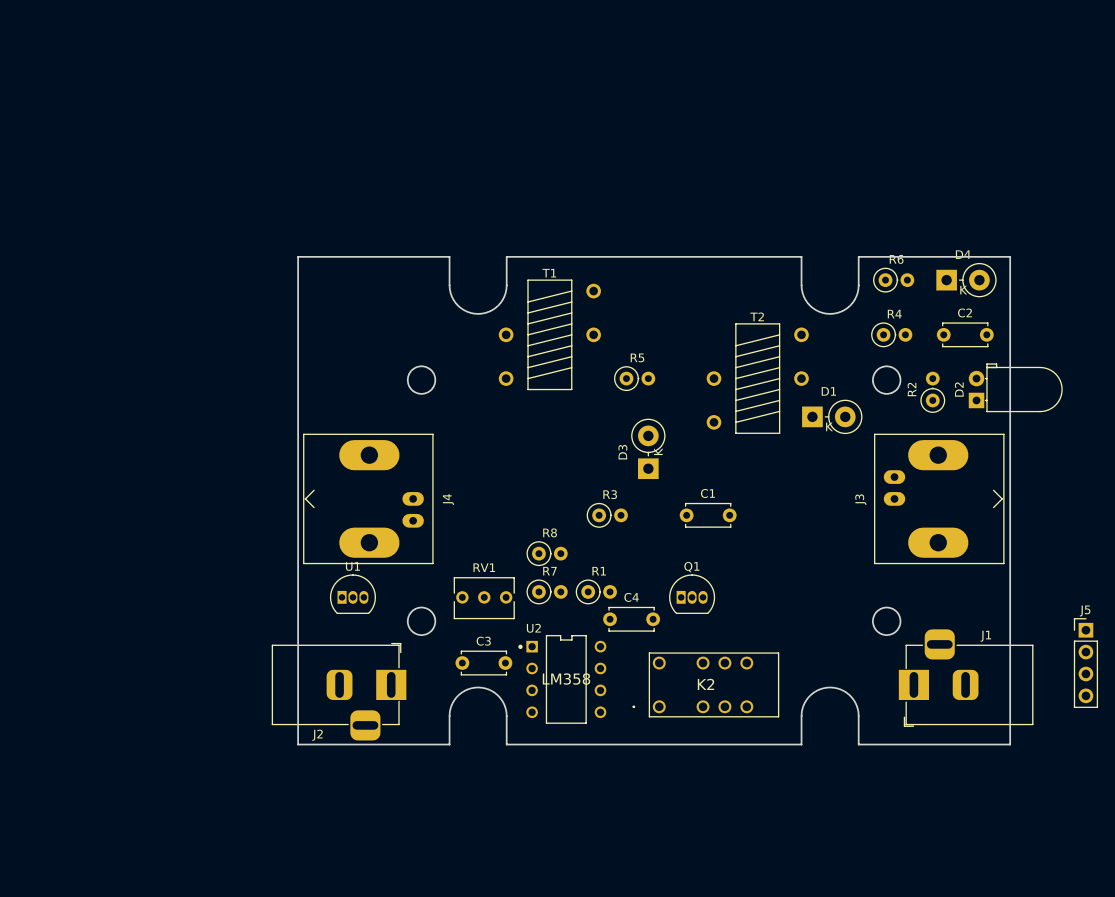
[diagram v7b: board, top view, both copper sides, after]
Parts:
- removed H1, H2, H3, H4: MountingHole, MountingHole:MountingHole_4.3mm_M4
- removed REF**10, REF**100, REF**1000, REF**1001, REF**1002, REF**1003, REF**1004, REF**101, REF**1010, REF**1012, REF**1013, REF**1014, REF**1015, REF**1017, REF**1019, REF**102, REF**1020, REF**1021, REF**1022, REF**1023, REF**1024, REF**1025, REF**1026, REF**1027, REF**1028, REF**1029, REF**103, REF**1030, REF**1031, REF**1033, REF**1035, REF**1036, REF**1037, REF**1038, REF**104, REF**1040, REF**1041, REF**1043, REF**1044, REF**1045, REF**1049, REF**105, REF**1050, REF**1051, REF**1052, REF**1053, REF**1054, REF**1057, REF**1058, REF**1059, REF**106, REF**1063, REF**1065, REF**1069, REF**107, REF**1071, REF**1073, REF**1074, REF**1075, REF**1076, REF**1078, REF**1079, REF**108, REF**1081, REF**1082, REF**1083, REF**1087, REF**1088, REF**1089, REF**109, REF**1090, REF**1091, REF**1092, REF**1095, REF**1096, REF**1097, REF**11, REF**1102, REF**1103, REF**1104, REF**1105, REF**1107, REF**112, REF**113, REF**1131, REF**1132, REF**1134, REF**1135, REF**114, REF**1141, REF**1145, REF**1147, REF**1148, REF**1149, REF**115, REF**1151, REF**1152, REF**1154, REF**1155, REF**1157, REF**1159, REF**1160, REF**1161, REF**1162, REF**1163, REF**1164, REF**1165, REF**1166, REF**1167, REF**1169, REF**1170, REF**1171, REF**1173, REF**1177, REF**1178, REF**1179, REF**118, REF**1180, REF**1181, REF**1183, REF**1185, REF**1186, REF**1187, REF**1188, REF**119, REF**1192, REF**1193, REF**1197, REF**1198, REF**1199, REF**12, REF**120, REF**1200, REF**1201, REF**1202, REF**1203, REF**1204, REF**1205, REF**1207, REF**1208, REF**121, REF**1211, REF**1212, REF**1213, REF**1214, REF**1215, REF**1216, REF**1217, REF**1218, REF**122, REF**1221, REF**1223, REF**1224, REF**1225, REF**1226, REF**1227, REF**123, REF**1230, REF**1231, REF**1235, REF**1236, REF**1237, REF**1238, REF**1239, REF**124, REF**1240, REF**1241, REF**1242, REF**1243, REF**1245, REF**1247, REF**1249, REF**125, REF**1250, REF**1251, REF**1252, REF**1253, REF**1254, REF**1255, REF**1258, REF**1259, REF**126, REF**1261, REF**1262, REF**1263, REF**1264, REF**1265, REF**1268, REF**1269, REF**1272, REF**1273, REF**1274, REF**1275, REF**1276, REF**1277, REF**1278, REF**1279, REF**128, REF**1280, REF**1281, REF**1282, REF**1283, REF**1284, REF**1285, REF**1287, REF**1288, REF**129, REF**1291, REF**1296, REF**1297, REF**1299, REF**13, REF**130, REF**1300, REF**1301, REF**1302, REF**1306, REF**1307, REF**131, REF**1311, REF**1312, REF**1313, REF**1314, REF**1315, REF**1316, REF**1317, REF**1318, REF**1319, REF**132, REF**1323, REF**1325, REF**1329, REF**133, REF**1330, REF**1334, REF**1335, REF**1336, REF**134, REF**1344, REF**1345, REF**135, REF**1352, REF**1353, REF**136, REF**1363, REF**1368, REF**137, REF**1372, REF**1373, REF**1374, REF**1377, REF**1378, REF**1379, REF**138, REF**1380, REF**1381, REF**1382, REF**1383, REF**1384, REF**1385, REF**1386, REF**1387, REF**1388, REF**1389, REF**139, REF**1390, REF**1393, REF**1394, REF**1395, REF**1399, REF**14, REF**140, REF**1400, REF**1401, REF**1406, REF**141, REF**142, REF**143, REF**1430, REF**1431, REF**1432, REF**1433, REF**144, REF**1441, REF**1442, REF**1443, REF**145, REF**146, REF**147, REF**15, REF**150, REF**151, REF**155, REF**156, REF**157, REF**158, REF**159, REF**165, REF**17, REF**179, REF**18, REF**180, REF**181, REF**182, REF**183, REF**184, REF**185, REF**186, REF**187, REF**19, REF**192, REF**193, REF**194, REF**195, REF**196, REF**197, REF**199, REF**2, REF**20, REF**200, REF**201, REF**202, REF**203, REF**204, REF**205, REF**206, REF**207, REF**208, REF**209, REF**21, REF**210, REF**211, REF**212, REF**213, REF**214, REF**215, REF**216, REF**217, REF**218, REF**219, REF**22, REF**220, REF**221, REF**222, REF**223, REF**224, REF**225, REF**228, REF**229, REF**23, REF**230, REF**231, REF**232, REF**233, REF**234, REF**235, REF**24, REF**25, REF**251, REF**252, REF**253, REF**259, REF**26, REF**260, REF**261, REF**262, REF**263, REF**264, REF**265, REF**266, REF**267, REF**268, REF**269, REF**27, REF**270, REF**271, REF**272, REF**273, REF**275, REF**276, REF**277, REF**278, REF**279, REF**28, REF**280, REF**281, REF**282, REF**283, REF**284, REF**285, REF**286, REF**287, REF**288, REF**289, REF**29, REF**290, REF**291, REF**292, REF**293, REF**294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: VIA-0.6mm, MyLibrary:VIA-0.6mm
- removed TP1: V Fwd, TestPoint:TestPoint_THTPad_4.0x4.0mm_Drill2.0mm
- removed TP2: V Refl, TestPoint:TestPoint_THTPad_4.0x4.0mm_Drill2.0mm
- D1, D3, D4: footprint Diode_THT:D_DO-41_SOD81_P10.16mm_Horizontal -> Diode_THT:D_DO-15_P3.81mm_Vertical_KathodeUp
- D2: footprint LED_THT:LED_D5.0mm -> LED_THT:LED_D5.0mm_Horizontal_O1.27mm_Z9.0mm
- K2: footprint KiCad:ATX209 -> ATX209:ATX209
- R1, R2, R3, R4, R5, R6, R7, R8: footprint Resistor_THT:R_Axial_DIN0207_L6.3mm_D2.5mm_P7.62mm_Horizontal -> Resistor_THT:R_Axial_DIN0207_L6.3mm_D2.5mm_P2.54mm_Vertical
- U2: footprint KiCAD:LM358 -> LM358:ON_Semiconductor-626-05-04_2015-P-MFG
- moved J5 89.4 mm to (205.1, 118.1)
- moved R5 61.1 mm to (151.8, 88.9)
- moved J4 56.9 mm to (127.0, 102.9)
- moved C4 56.6 mm to (149.9, 116.8), turned to 0 degrees
- moved R3 55.5 mm to (148.6, 104.8)
- moved C1 49.6 mm to (158.8, 104.8)
- moved D3 49.5 mm to (154.3, 99.4)
- moved J3 46.9 mm to (182.9, 102.9)
- moved D2 46.9 mm to (192.4, 91.4), turned to 90 degrees
- moved RV1 40.5 mm to (137.8, 114.3), turned to 0 degrees
- moved C3 38.8 mm to (132.7, 121.9), turned to 0 degrees
- moved T1 33.4 mm to (142.9, 76.2)
- moved J2 32.7 mm to (124.5, 124.5)
- moved R4 31.3 mm to (181.6, 83.8)
- moved R8 29.4 mm to (141.6, 109.2), turned to 0 degrees
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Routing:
- net +5V: track 154.0 -> 0.00 mm
- net +12V: track 89.0 -> 0.00 mm
- net Net-(D3-K): track 83.0 -> 0.00 mm
- net Net-(D4-K): track 74.4 -> 0.00 mm
- net Net-(D1-A): track 70.1 -> 0.00 mm
- net Net-(D3-A): track 65.6 -> 0.00 mm
- net Net-(J4-In): track 62.4 -> 0.00 mm
- net Net-(J3-In): track 46.6 -> 0.00 mm
- net Net-(D4-A): track 28.2 -> 0.00 mm
- net Net-(K2-NC_1): track 25.3 -> 0.00 mm
- net Net-(Q1-B): track 17.8 -> 0.00 mm
- net Net-(U2A--): track 16.5 -> 0.00 mm
- net Net-(U2B-+): track 11.4 -> 0.00 mm
- net Net-(R1-Pad2): track 10.4 -> 0.00 mm
- net Net-(D2-A): track 7.84 -> 0.00 mm
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- removed copper zone on B.Cu, net GND
- removed copper zone on F.Cu, net GND
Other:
- board size 100 x 100 mm -> 82.7 x 56.6 mm
- rule pad_to_mask_clearance: 0 -> 0.051
- board text added: "17.58"
- board text added: "28.00"
- board text added: "3.31"
- board text added: "54.00"
- board text added: "56.61"
- board text added: "6.63"
- board text added: "82.66"
- board text added: "[.13]"
- board text added: "[.26]"
- board text added: "[.69]"
- board text added: "[1.10]"
- board text added: "[2.13]"
- board text added: "[2.23]"
- board text added: "[3.25]"
- board text removed: "Step 1: Make It Work"
- board text removed: "Step 2: Make It Work Better"

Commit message: checkpoint progress on board layout
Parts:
- moved J5 30.8 mm to (175.3, 110.5)
- moved C4 12.6 mm to (141.6, 126.3), turned to 90 degrees
- moved R1 12.6 mm to (156.2, 104.8), turned to 180 degrees
- moved R7 10.2 mm to (136.5, 104.8)
- moved U2 10.2 mm to (144.8, 113.7)
- moved D1 5.95 mm to (175.9, 88.0), turned to -90 degrees
- moved T2 5.93 mm to (165.1, 75.7)
- moved R8 4.49 mm to (142.2, 104.8)
- moved K2 3.86 mm to (154.9, 123.2)
- moved J2 3.81 mm to (128.3, 124.5)
- moved J1 3.75 mm to (181.6, 125.7)
- moved D4 3.53 mm to (192.4, 78.1), turned to 180 degrees
- moved U1 3.24 mm to (121.9, 114.9), turned to 180 degrees
- moved C3 3.17 mm to (132.7, 118.7)
- moved Q1 2.01 mm to (158.8, 112.4)
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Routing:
- net +5V: track 0.00 -> 104.8 mm, vias 0 -> 2
- net Net-(D1-A): track 0.00 -> 59.7 mm, vias 0 -> 1
- net Net-(J4-In): track 0.00 -> 58.6 mm
- net +12V: track 0.00 -> 54.2 mm
- net Net-(D3-K): track 0.00 -> 49.0 mm
- net Net-(D4-K): track 0.00 -> 47.2 mm, vias 0 -> 1
- net Net-(J3-In): track 0.00 -> 43.0 mm
- net Net-(D3-A): track 0.00 -> 32.5 mm
- net Net-(K2-NC_1): track 0.00 -> 24.9 mm
- net Net-(D4-A): track 0.00 -> 21.3 mm
- net Net-(U2B-+): track 0.00 -> 18.6 mm
- net Net-(R1-Pad2): track 0.00 -> 15.0 mm, vias 0 -> 1
- net Net-(Q1-B): track 0.00 -> 9.20 mm
- net Net-(U2A--): track 0.00 -> 6.34 mm
- net Net-(D2-A): track 0.00 -> 5.08 mm
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- added copper zone on B.Cu, net GND
